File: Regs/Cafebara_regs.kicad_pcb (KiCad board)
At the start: 4 copper layers, 51 parts, among them U1 TDA38826XUMA1, U2 TDA38826XUMA1, U3 FAN49100AUC330X, U4 TLV74311PDBVR, U5 AP2210K-ADJ, U6 TPS61232DRC

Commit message: Largely finish positioning and routing
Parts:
- added TP1: EN, TestPoint:TestPoint_Pad_D1.5mm, F.Cu at (103.5, 113.8)
- C22, C23, C24, C25: footprint Capacitor_SMD:C_0402_1005Metric -> Capacitor_SMD:C_0603_1608Metric
- moved C23 3.51 mm to (95.8, 113.8), turned to 90 degrees
- moved C21 3.40 mm to (111.8, 110.8), turned to 180 degrees
- moved C18 1.12 mm to (122.8, 122.0), turned to -90 degrees
- moved C9 1.12 mm to (110.5, 122.0), turned to -90 degrees
- moved C20 1.00 mm to (115.5, 110.8)
- moved C17 0.79 mm to (122.5, 118.2)
- moved C8 0.79 mm to (110.2, 118.2)
- moved C22 0.35 mm to (101.8, 116.0)
- moved C24 0.35 mm to (101.8, 120.8)
- moved C25 0.35 mm to (95.8, 122.2)
- moved R6 0.35 mm to (122.5, 120.2)
- moved R7 0.35 mm to (122.5, 119.2)
- moved R2 0.35 mm to (110.2, 120.2)
- moved R3 0.35 mm to (110.2, 119.2)
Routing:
- net EN: track 6.63 -> 46.6 mm
- net Net-(U2-FB): track 4.44 -> 19.8 mm
- net Net-(U1-FB): track 4.44 -> 15.2 mm
- net +5V: track 0.00 -> 9.18 mm, vias 5 -> 35
- net Net-(U6-PG): track 0.00 -> 1.85 mm
- net 1V_BST: track 2.10 -> 3.29 mm
- net 1V15_BST: track 2.10 -> 3.29 mm
- net 1V_SS: track 3.08 -> 2.23 mm
- net 1V15_SS: track 3.13 -> 2.28 mm
- net GND: track 0.00 -> 0.40 mm, vias 33 -> 123
- net VCC: vias 37 -> 123
- net Net-(U2-SW): vias 8 -> 0
- net Net-(U1-SW): vias 8 -> 0
- net Net-(L4-Pad2): vias 0 -> 19
- net +3.3V: vias 6 -> 46
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- added copper zone on B.Cu, net +1V0
- added copper zone on F.Cu, net +1V1
- added copper zone on B.Cu, net +1V15
- added copper zone on F.Cu, net +1V25
- added copper zone on B.Cu, net +3.3V
- added copper zone on B.Cu, net +5V
- added copper zone on F.Cu, net Net-(L4-Pad2)
- added copper zone on In2.Cu, net Net-(L4-Pad2)
- added copper zone on B.Cu, net VCC
- removed copper zone on In2.Cu, net Net-(U1-SW)
- removed copper zone on In2.Cu, net Net-(U2-SW)
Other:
- board outline added: 43.5 x 28.5 mm
- board text added: "+1.15V"
- board text added: "+1.1V"
- board text added: "+1.25V"
- board text added: "+1V"
- board text added: "+3.3V"
- board text added: "+5V"
- board text added: "GND"
- board text added: "VCC"

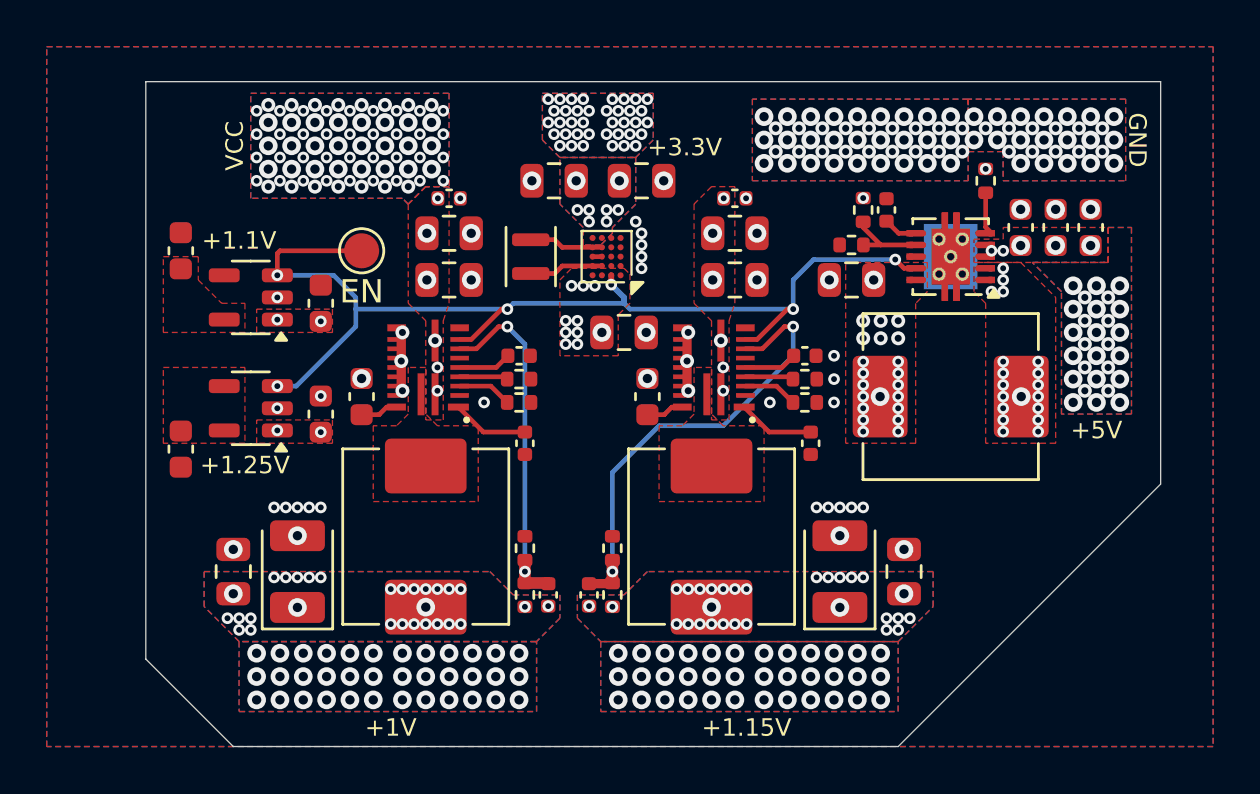
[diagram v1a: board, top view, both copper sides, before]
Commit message: Slight board outline adjustments
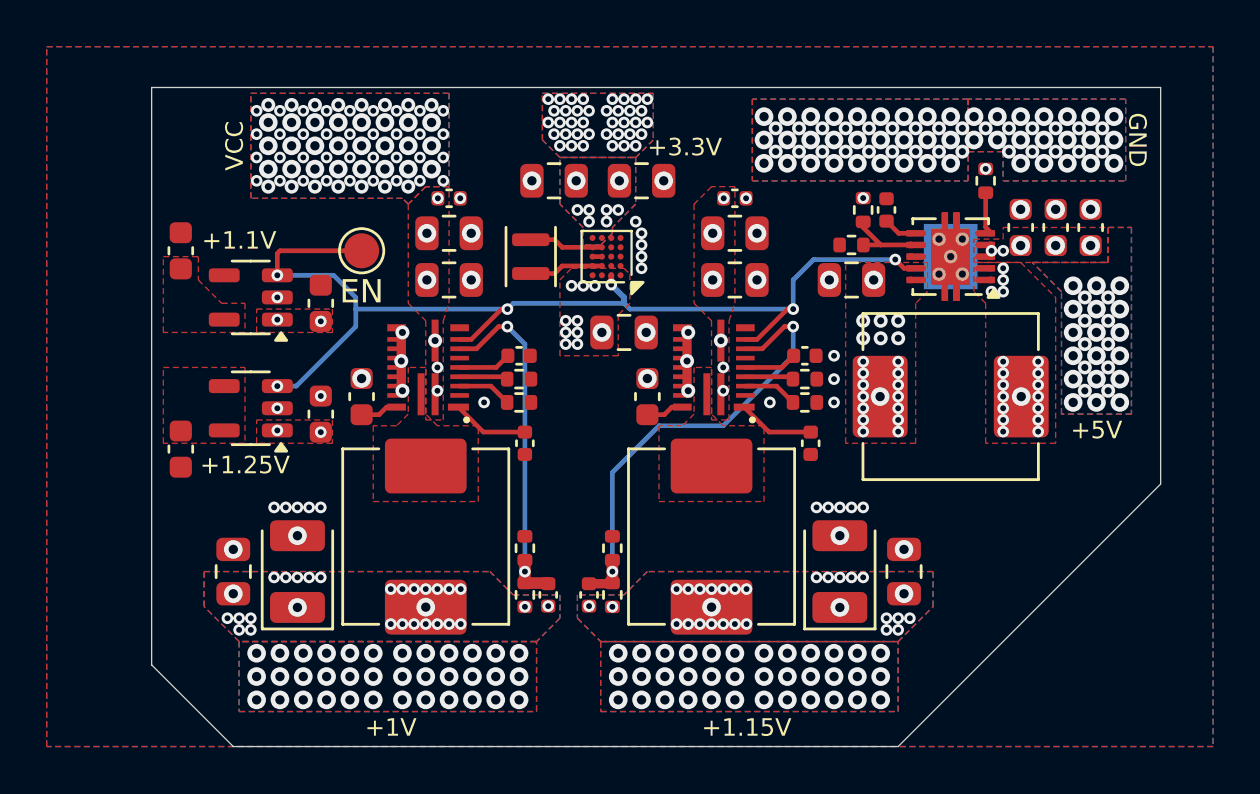
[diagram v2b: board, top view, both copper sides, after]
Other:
- board size 43.5 x 28.5 mm -> 43.2 x 28.2 mm

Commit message: Regulator board design finalisation
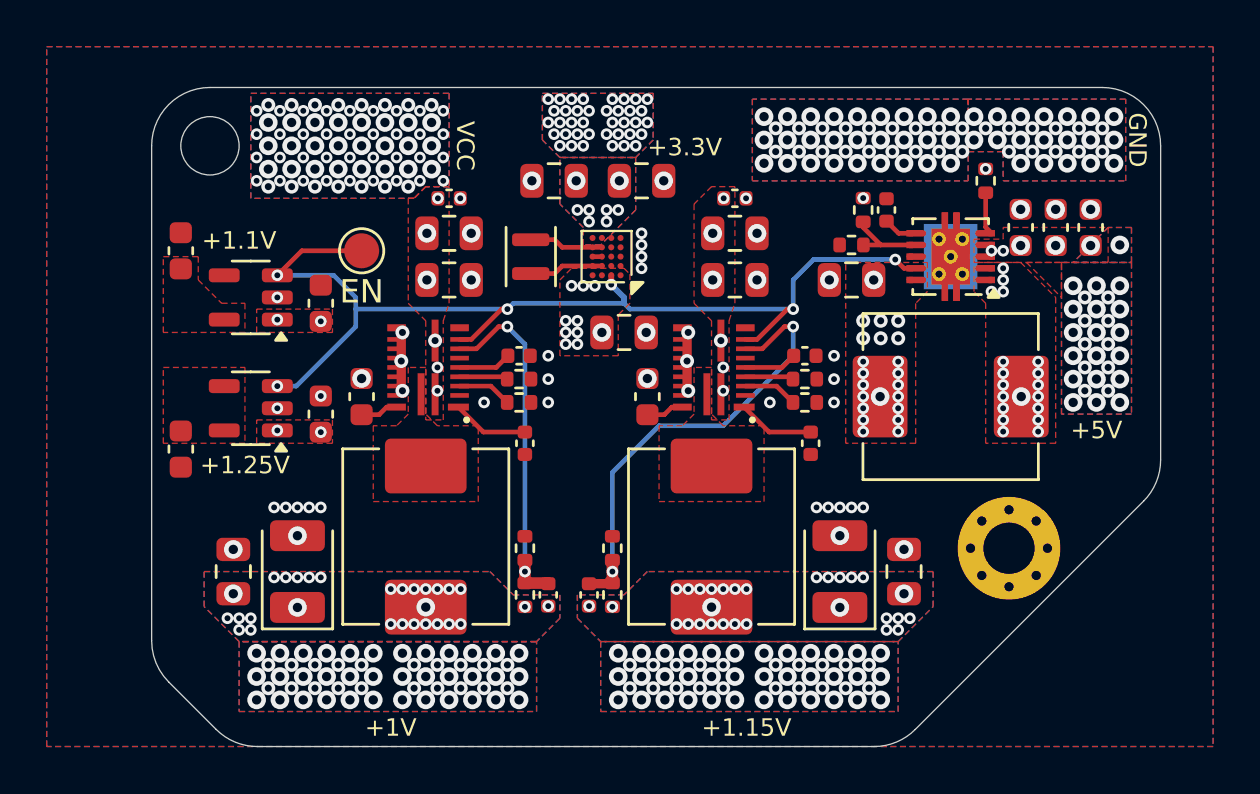
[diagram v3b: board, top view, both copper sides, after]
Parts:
- added H1: ~, MountingHole:MountingHole_2.2mm_M2_Pad_Via, F.Cu at (131.2, 126.5)
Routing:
- net EN: track 46.6 -> 46.1 mm
- net GND: vias 123 -> 125
- net +5V: vias 35 -> 36
- net +1V15: vias 65 -> 85
- net +1V0: vias 65 -> 85
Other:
- outline, holes or cut-outs redrawn

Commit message: Minor misc updates
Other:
- outline, holes or cut-outs redrawn

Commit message: Misc adjustments
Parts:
- moved R9 1.12 mm to (129.2, 111.2), turned to 0 degrees
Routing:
- net +5V: track 9.18 -> 8.51 mm
- net GND: vias 125 -> 128
- net +3.3V: vias 46 -> 8
- added copper zone on B.Cu, net Net-(L4-Pad2)

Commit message: Misc changes to cafebara, add temperature board
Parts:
- moved C26 0.25 mm to (124.5, 115.2)
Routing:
- net +5V: track 8.51 -> 8.26 mm, vias 36 -> 34
- net VCC: vias 123 -> 120
- net GND: vias 128 -> 152

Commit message: Misc improvements to several boards
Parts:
- moved TP1 9.01 mm to (96.0, 118.8), turned to 90 degrees
- moved C24 1.50 mm to (101.8, 122.2)
- moved C25 1.50 mm to (95.8, 123.8)
- moved U5 1.50 mm to (98.8, 122.0)
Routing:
- net EN: track 46.1 -> 48.7 mm
